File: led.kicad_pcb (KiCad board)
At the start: 2 copper layers, 100 x 100 mm, 122 parts, among them J1 Slip_ring_48V, J2 Slip_ring_I2C, J52 Jump_ID_1, J53 Jump_ID_2, J54 Test_Vds, J55 Test_sense, J56 Jump_ID_3, J57 Jump_ID_4, J58 Jump_ID_5, J59 Jump_ID_6, M1 Fan_LED_1, M2 Fan_LED_2, M3 Fan_LED_3, M4 Fan_LED_4, M5 Fan_LED_5, M6 Fan_LED_6, M7 Fan_FET_1, M8 Fan_FET_2, Q52 FKI10531, Q53 FKI10531, Q54 FKI10531, Q55 FKI10531, Q56 FKI10531, Q57 FKI10531, SW1 Reset, U1 ATmega328P-PU, U2 LM317_TO220, U3 LM78L05_TO92, U4 LM7812_TO220, U52 NJM4580, U53 NJM4580, U54 NJM4580, Y1 8MHz

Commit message: Update
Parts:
- removed M2: Fan_LED_2, Connector:FanPinHeader_1x03_P2.54mm_Vertical
- removed M3: Fan_LED_3, Connector:FanPinHeader_1x03_P2.54mm_Vertical
- removed M4: Fan_LED_4, Connector:FanPinHeader_1x03_P2.54mm_Vertical
- removed M5: Fan_LED_5, Connector:FanPinHeader_1x03_P2.54mm_Vertical
- removed M6: Fan_LED_6, Connector:FanPinHeader_1x03_P2.54mm_Vertical
- removed M7: Fan_FET_1, Connector:FanPinHeader_1x03_P2.54mm_Vertical
- removed M8: Fan_FET_2, Connector:FanPinHeader_1x03_P2.54mm_Vertical
- added REF**: Hole_slip_ring, Misc:Hole_slip_ring, F.Cu at (100.8, 100.8)
- M1: value Fan_LED_1 -> Fan
- moved D3 186.7 mm to (91.4, 104.1)
- moved C5 186.7 mm to (85.1, 101.6)
- moved U3 186.7 mm to (88.9, 100.3)
- moved J54 182.8 mm to (57.1, 68.6), turned to 180 degrees
- moved C7 172.7 mm to (118.0, 82.5)
- moved D4 172.7 mm to (110.5, 86.4)
- moved U4 172.7 mm to (110.5, 78.7)
- moved D1 169.2 mm to (94.0, 86.0), turned to 0 degrees
- moved C4 167.6 mm to (104.1, 83.8)
- moved C3 164.3 mm to (100.3, 78.5)
- moved C6 164.3 mm to (94.0, 69.5)
- moved D2 164.3 mm to (96.5, 78.4)
- moved R4 164.3 mm to (96.5, 82.2)
- moved R5 164.3 mm to (91.4, 78.4)
- moved U2 164.3 mm to (94.0, 74.6)
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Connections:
- U52 pad 5: Net-(RV53-Pad2) -> Net-(RV57-Pad2)
- U52 pad 6: Net-(RV55-Pad2) -> Net-(RV59-Pad2)
- U52 pad 7: Net-(D55-Pad2) -> Net-(D61-Pad2)
- U53 pad 1: Net-(D60-Pad2) -> Net-(D55-Pad2)
- U53 pad 2: Net-(RV58-Pad2) -> Net-(RV55-Pad2)
- U53 pad 3: Net-(RV56-Pad2) -> Net-(RV53-Pad2)
- U53 pad 5: Net-(RV57-Pad2) -> Net-(RV56-Pad2)
- U53 pad 6: Net-(RV59-Pad2) -> Net-(RV58-Pad2)
- U53 pad 7: Net-(D61-Pad2) -> Net-(D60-Pad2)

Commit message: Update
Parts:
- moved C7 15.4 mm to (105.4, 73.7), turned to 270 degrees
- moved D66 15.2 mm to (124.5, 118.1), turned to 270 degrees
- moved D4 14.8 mm to (97.8, 78.7), turned to 90 degrees
- moved R4 11.7 mm to (90.2, 72.4), turned to 90 degrees
- moved D2 11.5 mm to (85.1, 80.0), turned to 90 degrees
- moved U2 11.2 mm to (87.6, 83.8)
- moved C3 11.0 mm to (92.7, 86.4)
- moved M1 8.98 mm to (101.6, 71.1), turned to 180 degrees
- moved R70 8.89 mm to (127.0, 115.6)
- moved R5 8.67 mm to (92.7, 69.8)
- moved D1 8.67 mm to (92.7, 77.5), turned to 180 degrees
- moved C6 8.33 mm to (87.6, 74.9), turned to 0 degrees
- moved U4 8.03 mm to (102.9, 81.3), turned to 90 degrees
- moved C4 6.84 mm to (97.8, 81.3), turned to 270 degrees
- moved J2 3.59 mm to (114.3, 99.1), turned to 180 degrees
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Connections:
- R52 pad 1: /PWM1 -> /PWM5
- R53 pad 1: /PWM2 -> /PWM4
- R60 pad 1: /PWM3 -> /PWM6
- R61 pad 1: /PWM4 -> /PWM3
- R68 pad 1: /PWM5 -> /PWM2
- R69 pad 1: /PWM6 -> /PWM1
- U53 pad 1: Net-(D55-Pad2) -> Net-(D60-Pad2)
- U53 pad 2: Net-(RV55-Pad2) -> Net-(RV58-Pad2)
- U53 pad 3: Net-(RV53-Pad2) -> Net-(RV56-Pad2)
- U53 pad 5: Net-(RV56-Pad2) -> Net-(RV53-Pad2)
- U53 pad 6: Net-(RV58-Pad2) -> Net-(RV55-Pad2)
- U53 pad 7: Net-(D60-Pad2) -> Net-(D55-Pad2)
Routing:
- net GND: track 0.00 -> 416.5 mm
- net +48V: track 0.00 -> 251.3 mm, vias 0 -> 1
- net +12V: track 0.00 -> 109.7 mm
- net /PWM3: track 0.00 -> 88.3 mm
- net +5V: track 0.00 -> 66.5 mm
- net +24V: track 0.00 -> 56.0 mm
- net Net-(D55-Pad2): track 0.00 -> 36.1 mm
- net /PWM2: track 0.00 -> 32.6 mm
- net Net-(J54-Pad2): track 0.00 -> 32.1 mm
- net Net-(RV53-Pad2): track 0.00 -> 29.1 mm, vias 0 -> 1
- net Net-(RV62-Pad2): track 0.00 -> 28.6 mm
- net Net-(RV58-Pad2): track 0.00 -> 25.9 mm
- net Net-(RV63-Pad2): track 0.00 -> 25.7 mm
- net Net-(RV60-Pad2): track 0.00 -> 25.3 mm
- net /SDA: track 0.00 -> 24.0 mm
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- added copper zone on B.Cu, net Net-(HS1-Pad1)
- added copper zone on B.Cu, net Net-(HS2-Pad1)
- added copper zone on B.Cu, net Net-(HS3-Pad1)
- added copper zone on B.Cu, net Net-(HS4-Pad1)
- added copper zone on B.Cu, net Net-(HS5-Pad1)
- added copper zone on B.Cu, net Net-(HS6-Pad1)
- added copper zone on B.Cu, net Net-(Q55-Pad3)
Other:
- net class Default: clearance 0.2 -> 0.3
- rule trace_clearance: 0.2 -> 0.3

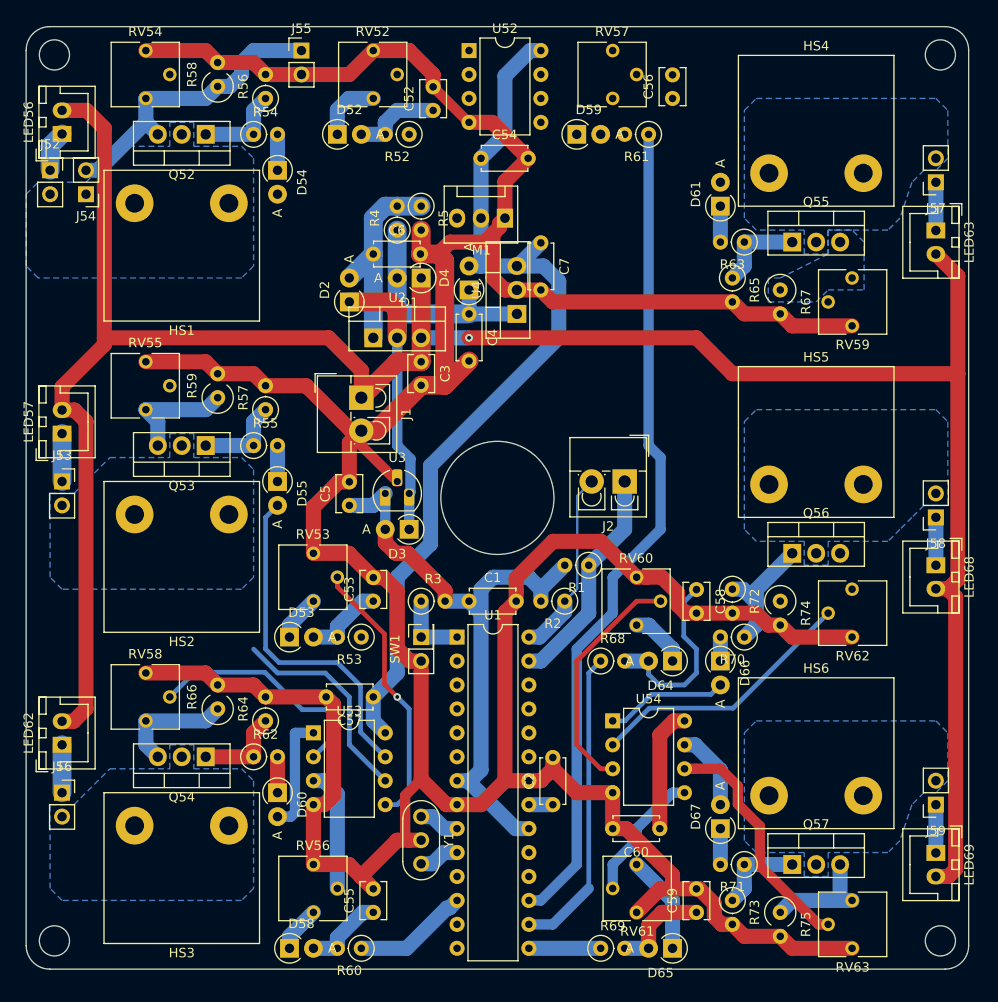
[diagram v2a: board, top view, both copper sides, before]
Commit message: PCB: Complete wiring
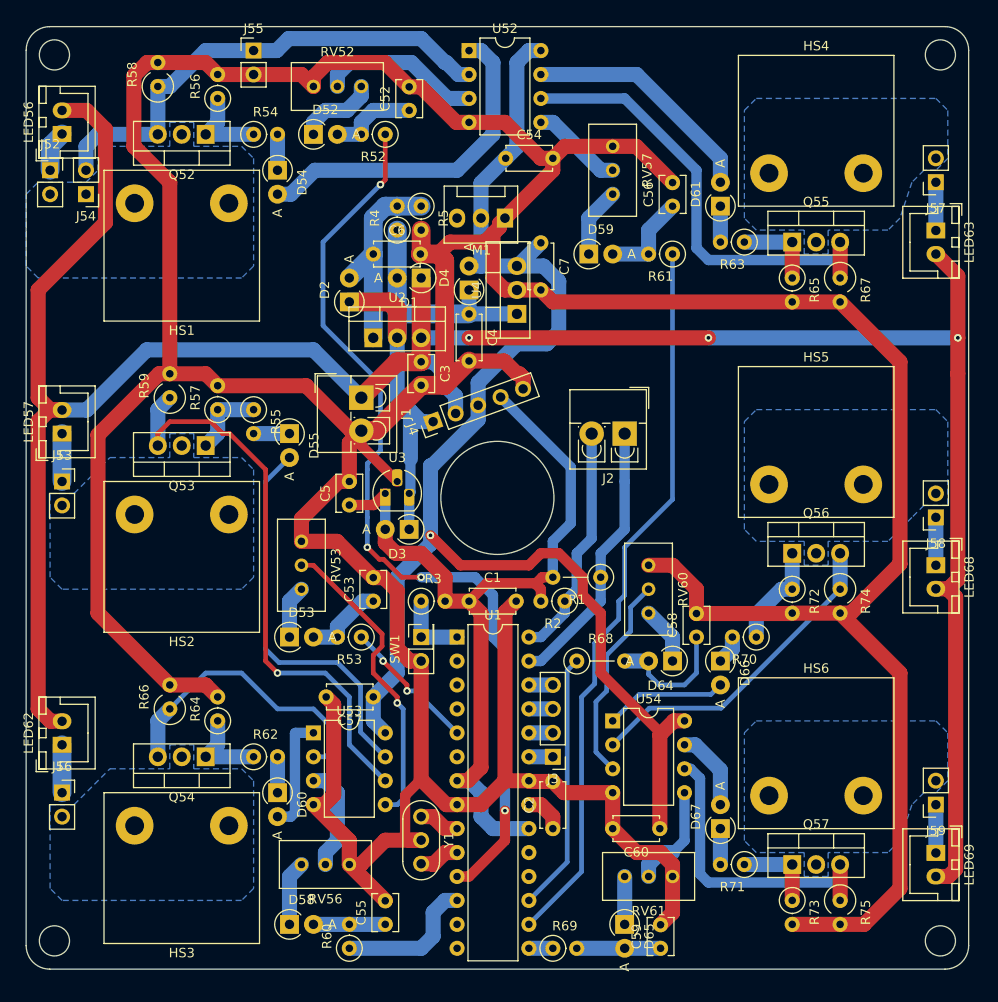
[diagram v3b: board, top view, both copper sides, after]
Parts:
- removed RV54, RV55, RV58, RV59, RV62, RV63: 30k, Potentiometer_THT:Potentiometer_Vishay_T73YP_Vertical
- added J3: Analog_input, Connector_PinHeader_2.54mm:PinHeader_1x04_P2.54mm_Vertical, F.Cu at (106.7, 128.3)
- added J4: Test_power, Connector_PinHeader_2.54mm:PinHeader_1x05_P2.54mm_Vertical, F.Cu at (94.0, 92.7)
- Q52, Q53, Q54, Q55, Q56, Q57: value FKI10531 -> EKI04027
- R1, R68: footprint Resistor_THT:R_Axial_DIN0207_L6.3mm_D2.5mm_P2.54mm_Vertical -> Resistor_THT:R_Axial_DIN0207_L6.3mm_D2.5mm_P5.08mm_Vertical
- RV52, RV53, RV56, RV57, RV60, RV61: value 30k -> 10k; footprint Potentiometer_THT:Potentiometer_Vishay_T73YP_Vertical -> Potentiometer_THT:Potentiometer_Bourns_3296W_Vertical
- U52, U53, U54: value NJM4580 -> NJM13404
- moved R61 13.0 mm to (119.4, 74.9)
- moved D59 12.8 mm to (110.5, 74.9)
- moved C56 11.4 mm to (119.4, 69.8)
- moved RV57 10.2 mm to (113.0, 68.6), turned to 270 degrees
- moved R74 6.48 mm to (137.2, 110.5)
- moved R75 6.48 mm to (137.2, 143.5)
- moved R67 6.48 mm to (137.2, 77.5)
- moved R58 6.35 mm to (64.8, 57.1)
- moved R65 6.35 mm to (132.1, 77.5)
- moved R72 6.35 mm to (132.1, 110.5)
- moved R73 6.35 mm to (132.1, 143.5)
- moved D65 5.68 mm to (114.3, 146.1), turned to 270 degrees
- moved C59 5.39 mm to (118.1, 148.6)
- moved RV56 5.24 mm to (80.0, 139.7), turned to 180 degrees
- moved D55 5.24 mm to (78.7, 94.0)
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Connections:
- R61 pad 1: /PWM3 -> /PWM2
- R68 pad 1: /PWM2 -> /PWM3
- U1 pad 23: (no net) -> /ADC0
- U1 pad 24: (no net) -> /ADC1
- U1 pad 25: (no net) -> /ADC2
- U1 pad 26: (no net) -> /ADC3
- U52 pad 2: Net-(RV54-Pad2) -> Net-(J54-Pad2)
- U52 pad 6: Net-(RV59-Pad2) -> Net-(Q55-Pad3)
- U53 pad 2: Net-(RV58-Pad2) -> Net-(Q54-Pad3)
- U53 pad 6: Net-(RV55-Pad2) -> Net-(Q53-Pad3)
- U54 pad 2: Net-(RV62-Pad2) -> Net-(Q56-Pad3)
- U54 pad 6: Net-(RV63-Pad2) -> Net-(Q57-Pad3)
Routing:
- net GND: track 416.5 -> 538.2 mm
- net /PWM5: track 0.00 -> 98.3 mm, vias 0 -> 4
- net /PWM3: track 88.3 -> 27.5 mm
- net Net-(Q53-Pad3): track 12.5 -> 62.2 mm, vias 0 -> 1
- net Net-(Q55-Pad3): track 0.00 -> 49.0 mm
- net /PWM2: track 32.6 -> 77.4 mm
- net +12V: track 109.7 -> 150.9 mm, vias 0 -> 1
- net Net-(D54-Pad2): track 0.00 -> 36.2 mm
- net Net-(Q56-Pad3): track 0.00 -> 34.8 mm
- net Net-(RV62-Pad2): track 28.6 -> 0.00 mm
- net Net-(RV58-Pad2): track 25.9 -> 0.00 mm
- net Net-(RV63-Pad2): track 25.7 -> 0.00 mm
- net Net-(D61-Pad2): track 0.00 -> 25.3 mm
- net +5V: track 66.5 -> 90.1 mm
- net Net-(RV55-Pad2): track 22.7 -> 0.00 mm
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- removed copper zone on B.Cu, net Net-(Q55-Pad3)
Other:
- net class Default: trace_width 0.25 -> 0.3
- rule trace_min: 0.2 -> 0.3

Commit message: Update
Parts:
- moved J54 7.41 mm to (61.0, 62.2)
- moved R59 1.80 mm to (64.8, 91.4)
- moved R66 1.80 mm to (64.8, 124.5)
- moved J52 1.80 mm to (54.6, 67.3)
- moved R57 1.27 mm to (69.8, 91.4)
- moved R64 1.27 mm to (69.8, 124.5)
- moved R58 1.27 mm to (64.8, 58.4)
- moved RV53 1.27 mm to (81.3, 110.5)
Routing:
- net GND: track 538.2 -> 499.5 mm
- net Net-(HS1-Pad1): track 0.00 -> 7.87 mm
- net Net-(J54-Pad2): track 52.5 -> 46.1 mm
- net +48V: track 265.4 -> 259.7 mm
- net Net-(Q53-Pad3): track 62.2 -> 59.9 mm, vias 1 -> 3
- net Net-(RV53-Pad2): track 32.9 -> 31.7 mm
- net Net-(Q54-Pad3): track 31.9 -> 32.7 mm
- net Net-(Q53-Pad1): track 8.15 -> 8.89 mm
- net Net-(J52-Pad1): track 4.38 -> 5.12 mm
- net Net-(Q54-Pad1): track 9.42 -> 8.89 mm
- net Net-(D53-Pad1): track 5.61 -> 6.13 mm
- net Net-(D55-Pad2): track 41.7 -> 41.2 mm

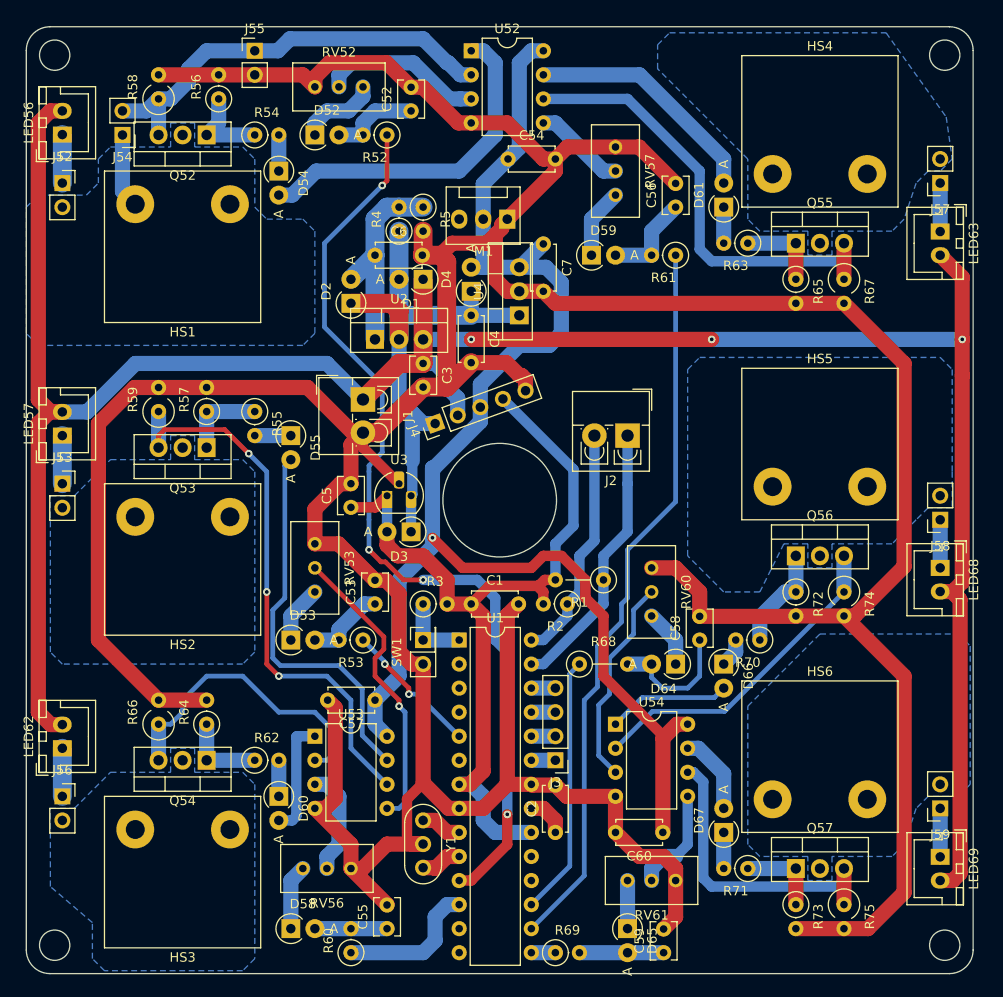
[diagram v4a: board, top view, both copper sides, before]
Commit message: PCB: Add fill zones of power
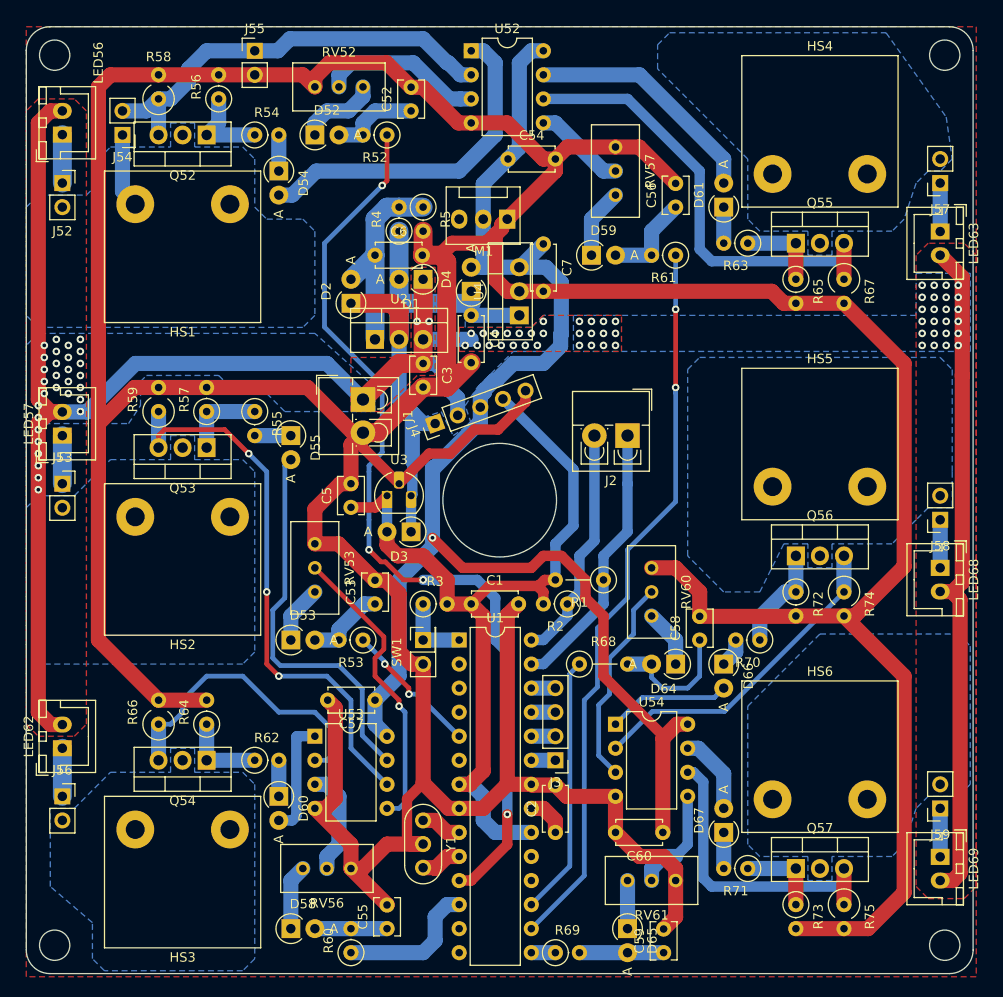
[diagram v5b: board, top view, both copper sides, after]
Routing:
- net GND: track 499.5 -> 552.4 mm
- net +48V: track 259.7 -> 207.9 mm, vias 3 -> 83
- net /PWM2: vias 0 -> 2
- added copper zone on B.Cu, net +48V
- added copper zone on F.Cu, net +48V
- added copper zone on F.Cu, net GND
